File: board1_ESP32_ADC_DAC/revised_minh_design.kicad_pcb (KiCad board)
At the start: 2 copper layers, 137.7 x 59.9 mm, 15 parts, among them J1 Conn_01x03_Male, J2 Conn_01x07_Male, U1 ESP32-DevKit-C, U2 LM7805_TO220, U3 NE5532, U4 CB101

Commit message: -
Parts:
- removed C3: 0.1uF, Capacitor_THT:C_Disc_D6.0mm_W2.5mm_P5.00mm
- removed D1: TZX3V6A-TR, Diode_THT:D_DO-35_SOD27_P7.62mm_Horizontal
- removed D2: LED, LED_THT:LED_D3.0mm_Clear
- removed J2: Conn_01x07_Male, Connector_PinSocket_2.54mm:PinSocket_1x07_P2.54mm_Vertical
- removed R1, R2: 10k, Resistor_THT:R_Axial_DIN0309_L9.0mm_D3.2mm_P15.24mm_Horizontal
- removed R3: 1K, Resistor_THT:R_Axial_DIN0309_L9.0mm_D3.2mm_P15.24mm_Horizontal
- removed R4: 4.7k, Resistor_THT:R_Axial_DIN0309_L9.0mm_D3.2mm_P15.24mm_Horizontal
- removed U3: NE5532, Package_DIP:DIP-8_W7.62mm
- removed U4: CB101, Library:CB101
- moved J1 70.2 mm to (40.0, 10.0), turned to 0 degrees
- moved C2 65.8 mm to (25.0, 20.0), turned to 0 degrees
- moved C1 55.6 mm to (55.0, 15.0), turned to 0 degrees
- moved U1 51.6 mm to (84.5, 81.2), turned to 90 degrees
- moved U2 34.7 mm to (24.9, 82.6)
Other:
- board size 137.7 x 59.9 mm -> 100 x 100 mm
- board text removed: "+12V"

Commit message: ADC_DAC
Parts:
- added C10: 2.2uF, Capacitor_SMD:C_0805_2012Metric_Pad1.18x1.45mm_HandSolder, F.Cu at (101.8, 49.1)
- added C11: 0.1uF, Capacitor_SMD:C_0805_2012Metric_Pad1.18x1.45mm_HandSolder, F.Cu at (113.9, 66.9)
- added C12: 2.2uF, Capacitor_SMD:C_0805_2012Metric_Pad1.18x1.45mm_HandSolder, F.Cu at (108.3, 43.8)
- added C13: 1nF, Capacitor_SMD:C_0805_2012Metric_Pad1.18x1.45mm_HandSolder, F.Cu at (111.2, 49.6)
- added C14: 1uF, Capacitor_SMD:C_0805_2012Metric_Pad1.18x1.45mm_HandSolder, F.Cu at (130.6, 51.4)
- added C3: 10uF, Capacitor_SMD:C_0805_2012Metric_Pad1.18x1.45mm_HandSolder, B.Cu at (108.0, 62.3)
- added C4: 0.1uF, Capacitor_SMD:C_0805_2012Metric_Pad1.18x1.45mm_HandSolder, B.Cu at (104.2, 53.7)
- added C5: 0.1uF, Capacitor_SMD:C_0805_2012Metric_Pad1.18x1.45mm_HandSolder, B.Cu at (106.0, 62.3)
- added C6: 0.1uF, Capacitor_SMD:C_0805_2012Metric_Pad1.18x1.45mm_HandSolder, B.Cu at (107.2, 56.4)
- added C7: 0.1uF, Capacitor_SMD:C_0805_2012Metric_Pad1.18x1.45mm_HandSolder, B.Cu at (106.0, 66.1)
- added C8: 10uF, Capacitor_SMD:C_0805_2012Metric_Pad1.18x1.45mm_HandSolder, B.Cu at (109.2, 56.4)
- added C9: 10uF, Capacitor_SMD:C_0805_2012Metric_Pad1.18x1.45mm_HandSolder, B.Cu at (108.0, 66.1)
- added J2: Conn_01x08_Male, Connector_PinSocket_2.54mm:PinSocket_1x08_P2.54mm_Vertical, F.Cu at (115.9, 42.4)
- added J3: Conn_01x08_Male, Connector_PinSocket_2.54mm:PinSocket_1x08_P2.54mm_Vertical, F.Cu at (120.8, 76.0)
- added J4: Conn_01x08_Male, Connector_PinSocket_2.54mm:PinSocket_1x08_P2.54mm_Vertical, F.Cu at (141.1, 48.6)
- added R1: 0, Resistor_SMD:R_0805_2012Metric_Pad1.20x1.40mm_HandSolder, B.Cu at (97.7, 56.5)
- added R2: 50, Resistor_SMD:R_0805_2012Metric_Pad1.20x1.40mm_HandSolder, F.Cu at (111.2, 45.9)
- added R3: 0, Resistor_SMD:R_0805_2012Metric_Pad1.20x1.40mm_HandSolder, F.Cu at (120.2, 65.9)
- added R4: 0, Resistor_SMD:R_0805_2012Metric_Pad1.20x1.40mm_HandSolder, F.Cu at (129.5, 47.6)
- added U3: MCP1754S-3302xCB, Package_TO_SOT_SMD:SOT-23, B.Cu at (104.2, 56.5)
- added U4: MCP1825S-3.3V, Package_TO_SOT_SMD:SOT-223-3_TabPin2, B.Cu at (100.6, 64.0)
- added U5: MCP1501-33xSN, Package_SO:SOIC-8_3.9x4.9mm_P1.27mm, F.Cu at (106.5, 47.5)
- added U6: MCP3464R, Package_SO:TSSOP-20_4.4x6.5mm_P0.65mm, F.Cu at (133.1, 57.1)
- added U7: MCP3464R, Package_SO:TSSOP-20_4.4x6.5mm_P0.65mm, F.Cu at (128.6, 68.7)
- added U8: DAC8568IAPW, Package_SO:TSSOP-16-1EP_4.4x5mm_P0.65mm, F.Cu at (124.0, 50.4)
- added X1: ECS-2520MVLC-049-BN-TR, Oscillator:Oscillator_SMD_ECS_2520MV-xxx-xx-4Pin_2.5x2.0mm, F.Cu at (116.6, 66.6)
- C1, C2: footprint Capacitor_THT:C_Disc_D6.0mm_W2.5mm_P5.00mm -> Capacitor_SMD:C_0805_2012Metric_Pad1.18x1.45mm_HandSolder
- moved J1 94.4 mm to (108.6, 74.9), turned to 90 degrees
- moved C2 90.4 mm to (98.8, 72.2)
- moved U2 78.9 mm to (103.4, 74.8), turned to 180 degrees
- moved C1 74.4 mm to (102.6, 72.2), turned to 180 degrees
- moved U1 31.1 mm to (65.0, 57.0)
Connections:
- U1 pad 25: unconnected-(U1-Pad25) -> MDAT
- U1 pad 26: unconnected-(U1-Pad26) -> ~{ADC2_CS}
- U1 pad 27: unconnected-(U1-Pad27) -> ~{ADC1_CS}
- U1 pad 28: DAC_SIG -> unconnected-(U1-Pad28)
- U1 pad 30: unconnected-(U1-Pad30) -> ~{DAC_CS}
- U1 pad 31: unconnected-(U1-Pad31) -> SK
- U1 pad 32: unconnected-(U1-Pad32) -> SI
- U1 pad 34: unconnected-(U1-Pad34) -> SO
- U1 pad 8: unconnected-(U1-Pad8) -> LDAC
- U1 pad 9: unconnected-(U1-Pad9) -> ~{CLR}
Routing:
- net ~{DAC_CS}: track 0.00 -> 50.1 mm
- net SK: track 0.00 -> 46.9 mm
- net SI: track 0.00 -> 44.7 mm
- net SO: track 0.00 -> 39.5 mm
- net +5V: track 0.00 -> 26.0 mm, vias 0 -> 3
- net GNDA: track 0.00 -> 19.5 mm, vias 0 -> 5
- net Earth: track 0.00 -> 16.6 mm, vias 0 -> 10
- net VoutA: track 0.00 -> 13.6 mm, vias 0 -> 1
- net ADC2_8: track 0.00 -> 13.3 mm, vias 0 -> 1
- net VoutB: track 0.00 -> 12.7 mm
- net ADC2_7: track 0.00 -> 12.0 mm
- net ADC2_1: track 0.00 -> 11.0 mm
- net VoutC: track 0.00 -> 10.7 mm, vias 0 -> 1
- net VoutD: track 0.00 -> 10.2 mm
- net VoutF: track 0.00 -> 9.68 mm
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- added copper zone on B.Cu, net Earth
- added copper zone on In1.Cu, net Earth
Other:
- board size 100 x 100 mm -> 94 x 39 mm
- copper layers 2 -> 4

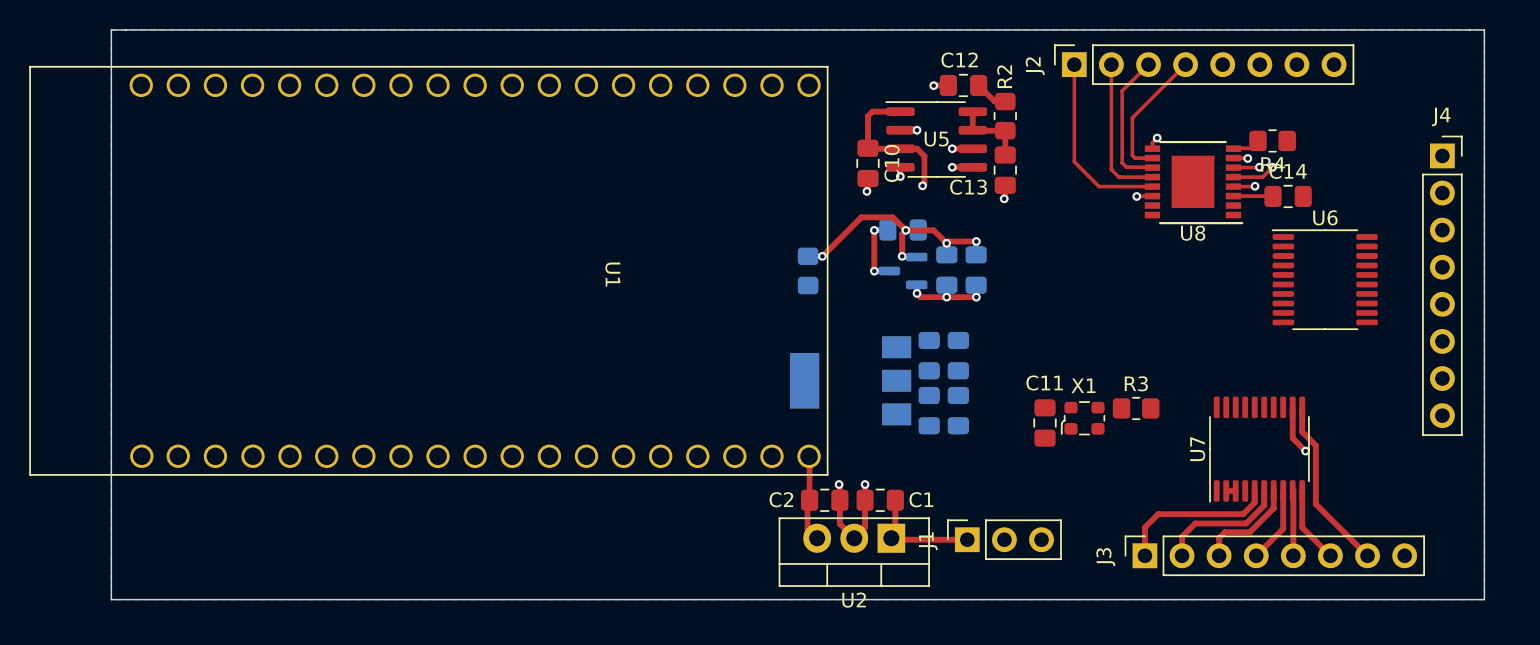
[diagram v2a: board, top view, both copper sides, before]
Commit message: components routing mostly finished for DAC/ADC board
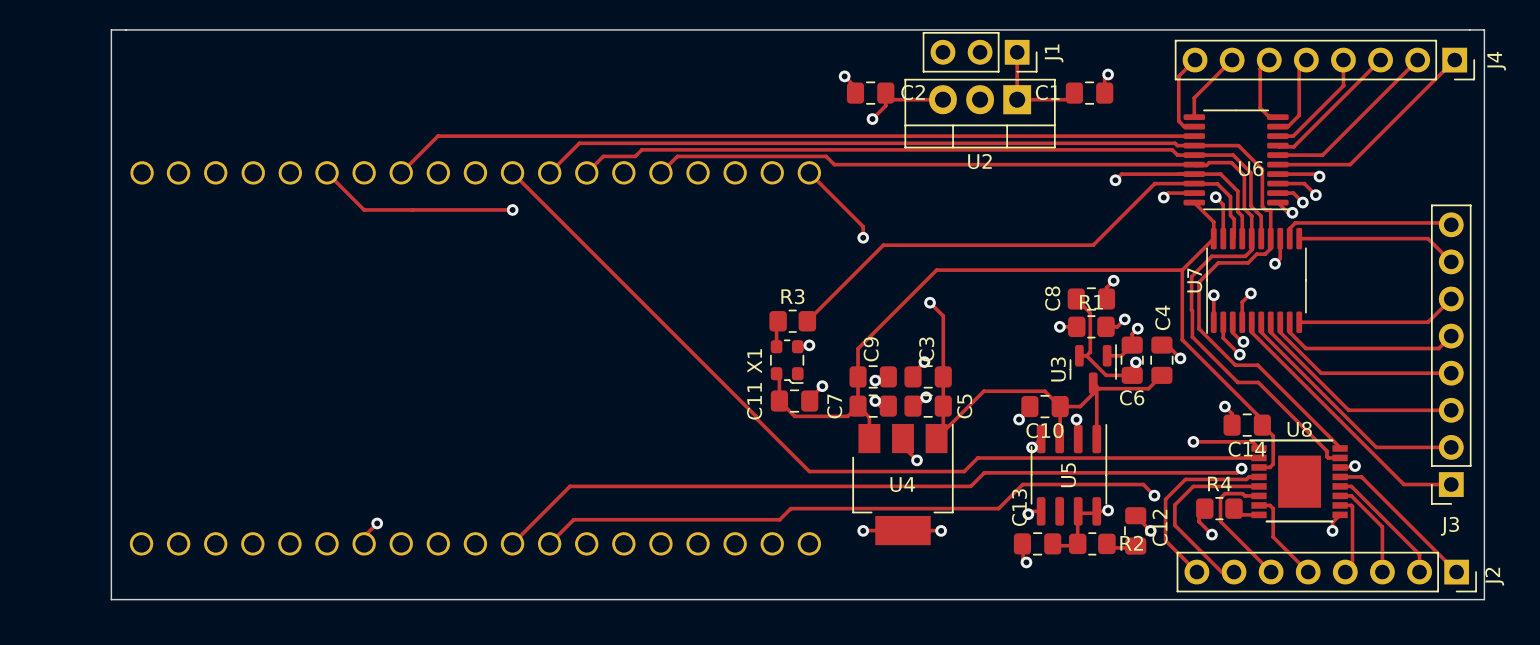
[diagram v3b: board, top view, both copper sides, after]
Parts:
- C3, C4, C5, C6, C7, C8, C9, R1, U3, U4: moved to F.Cu
- U1: moved to B.Cu
- moved J2 43.5 mm to (142.1, 77.1), turned to -90 degrees
- moved J1 33.5 mm to (112.0, 41.5), turned to -90 degrees
- moved C12 32.7 mm to (120.1, 74.3), turned to 90 degrees
- moved C1 31.3 mm to (117.0, 44.3), turned to 0 degrees
- moved U2 31.2 mm to (112.0, 44.8)
- moved R2 29.9 mm to (117.2, 75.2), turned to 0 degrees
- moved C2 28.1 mm to (102.0, 44.3), turned to 180 degrees
- moved C13 25.7 mm to (113.4, 75.2), turned to 180 degrees
- moved R4 25.4 mm to (125.9, 72.8), turned to 0 degrees
- moved U5 24.7 mm to (115.6, 70.5), turned to -90 degrees
- moved R3 24.3 mm to (96.6, 59.9)
- moved U8 21.8 mm to (131.3, 70.9), turned to 0 degrees
- moved J3 21.5 mm to (141.7, 71.1), turned to 180 degrees
- moved X1 20.7 mm to (96.3, 62.6), turned to 180 degrees
- moved C10 20.6 mm to (113.9, 65.8), turned to 180 degrees
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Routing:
- net MDAT: track 0.00 -> 70.9 mm, vias 0 -> 2
- net ~{ADC2_CS}: track 0.00 -> 68.7 mm, vias 0 -> 1
- net +3V3: track 2.71 -> 62.0 mm
- net ~{ADC1_CS}: track 0.00 -> 55.3 mm
- net ~{CLR}: track 7.06 -> 61.3 mm, vias 1 -> 2
- net LDAC: track 0.00 -> 52.9 mm, vias 0 -> 2
- net +3.3VDAC: track 5.17 -> 51.5 mm, vias 0 -> 4
- net CLK: track 0.00 -> 36.3 mm
- net +5V: track 26.0 -> 58.7 mm
- net SK: track 46.9 -> 78.4 mm
- net SO: track 39.5 -> 69.2 mm
- net +3.3VA: track 6.42 -> 29.7 mm
- net Earth: track 16.6 -> 34.7 mm, vias 10 -> 23
- net ADC1_1: track 0.00 -> 15.1 mm
- net ADC1_2: track 0.00 -> 12.3 mm
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- added copper zone on In1.Cu, net GNDA
- removed copper zone on B.Cu, net Earth

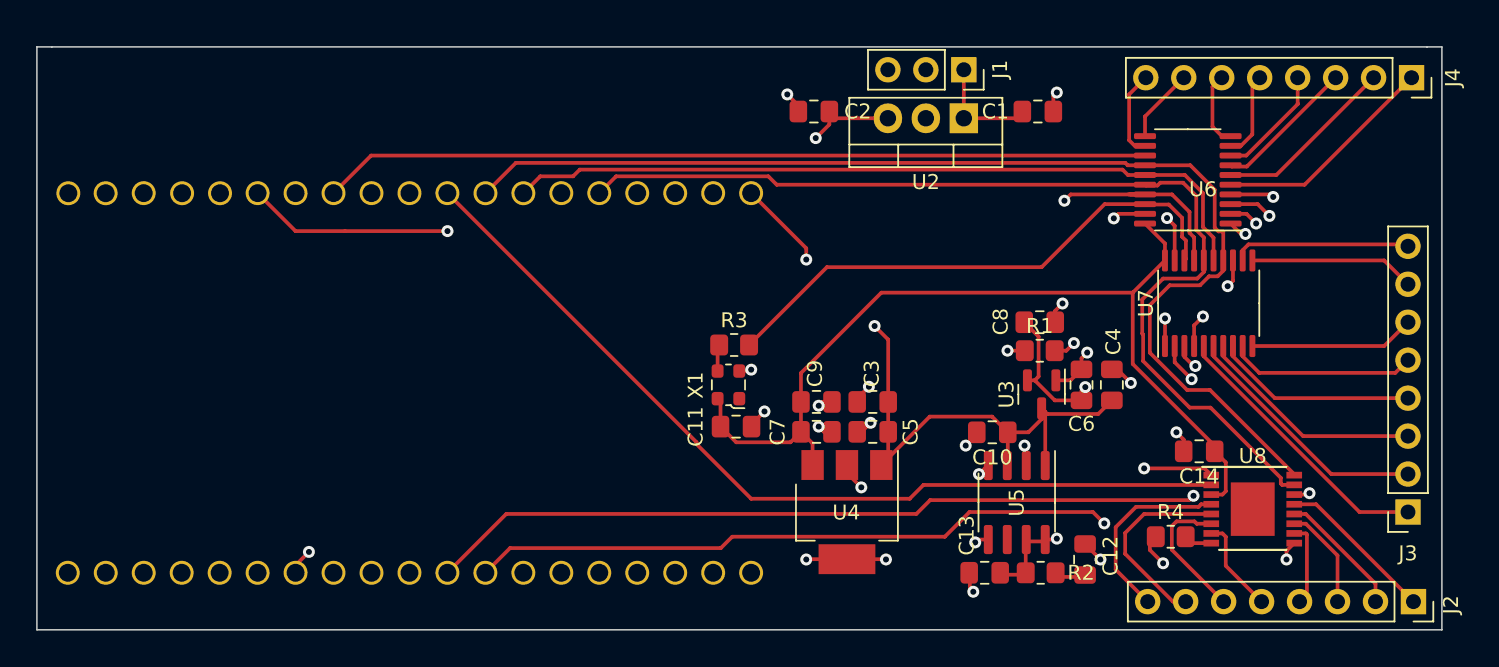
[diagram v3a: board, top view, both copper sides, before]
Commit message: components routing mostly finished for DAC/ADC board
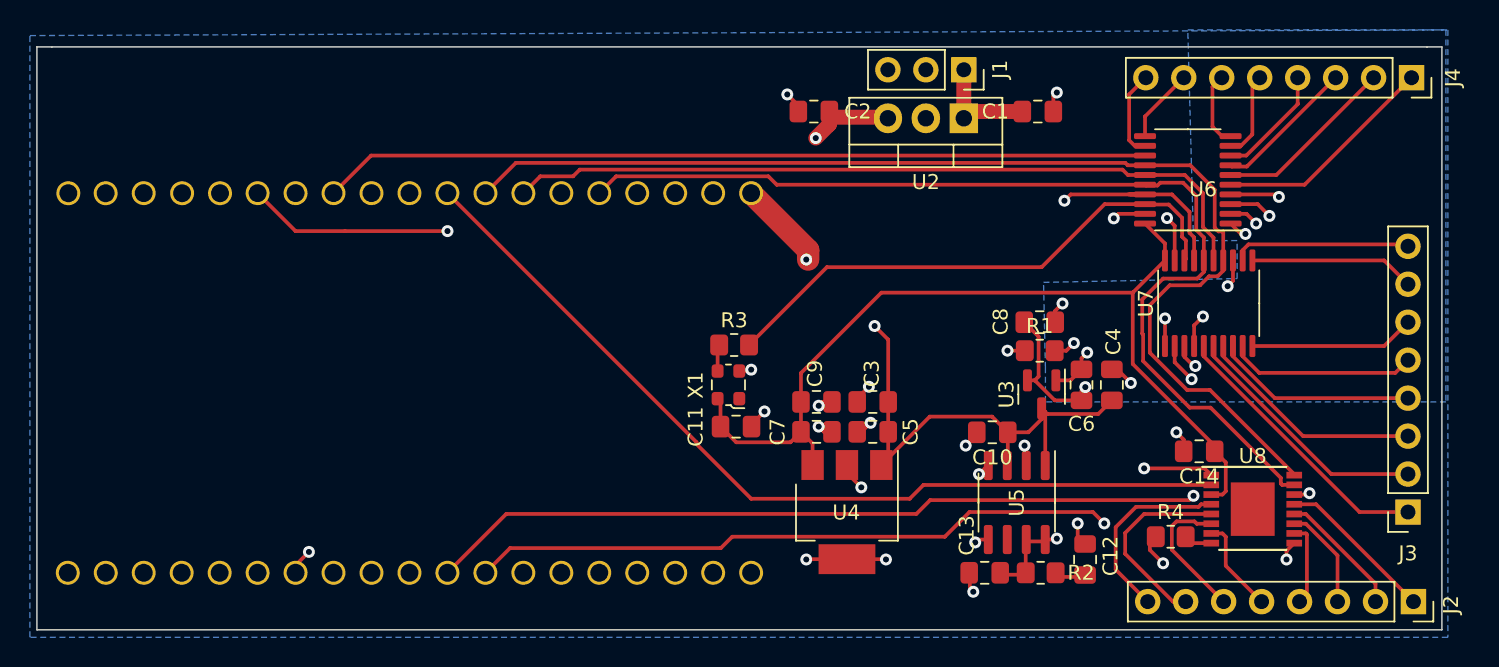
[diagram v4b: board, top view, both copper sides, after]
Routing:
- net +12V: track 7.35 -> 7.99 mm
- added copper zone on In2.Cu, net +12V
- added copper zone on In2.Cu, net +3.3VDAC
- added copper zone on In2.Cu, net +5V
- added copper zone on B.Cu, net Earth
- added copper zone on B.Cu, net GNDA

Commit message: minor adjustments
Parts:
- moved C8 0.15 mm to (117.0, 58.3)
- moved C3 0.13 mm to (105.9, 63.9)
- moved C9 0.13 mm to (102.2, 63.9)
- moved U4 0.13 mm to (104.2, 71.2)
- moved C5 0.13 mm to (105.9, 65.9)
- moved C7 0.13 mm to (102.2, 65.9)
- moved R1 0.05 mm to (117.0, 60.3)
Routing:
- net +12V: track 7.99 -> 2.76 mm, vias 0 -> 1
- net GNDA: track 17.2 -> 19.1 mm
- net Earth: track 34.8 -> 36.0 mm, vias 23 -> 24

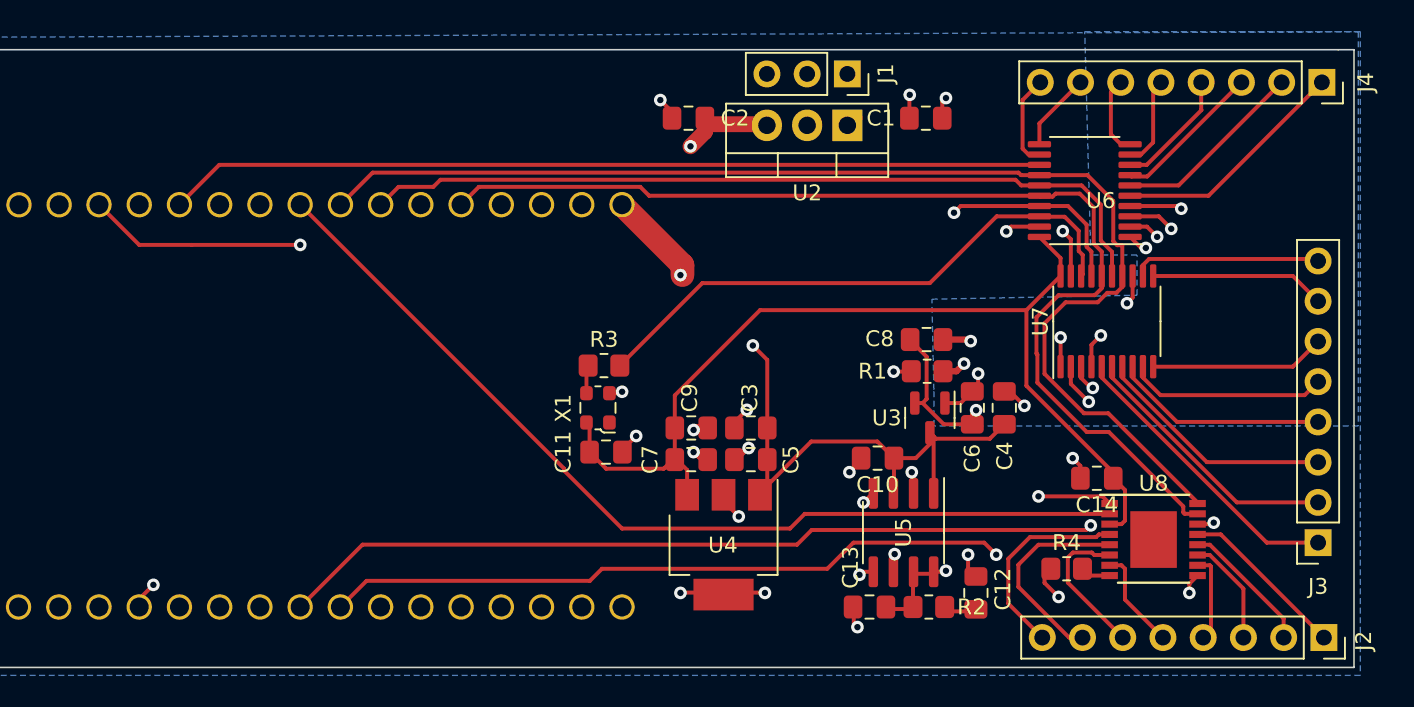
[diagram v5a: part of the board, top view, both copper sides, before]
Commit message: resolved DRC errors and most warnings
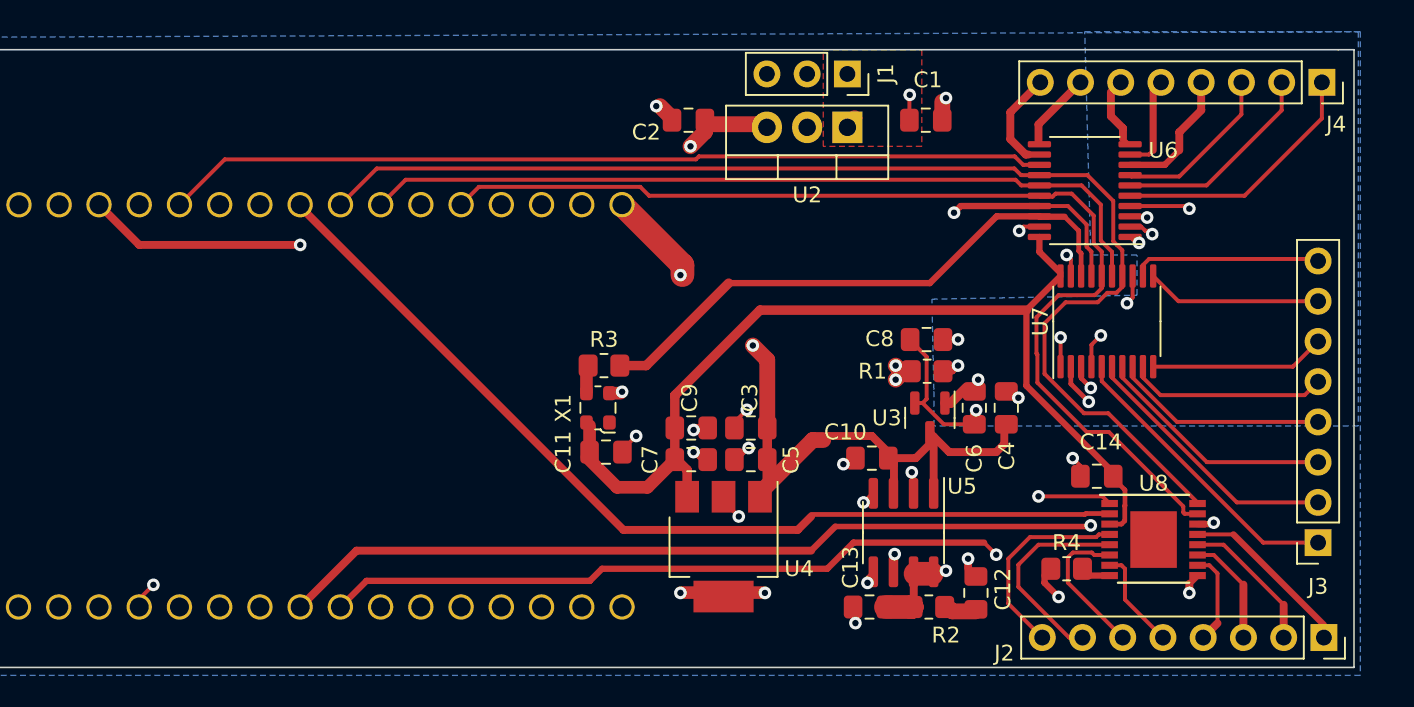
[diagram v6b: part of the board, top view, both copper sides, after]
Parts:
- moved C10 0.36 mm to (113.6, 65.8)
- moved C1 0.13 mm to (117.0, 44.5)
- moved C2 0.13 mm to (102.0, 44.5)
- moved U2 0.13 mm to (112.0, 44.9)
- moved C14 0.13 mm to (127.8, 66.9)
- moved C4 0.13 mm to (122.0, 62.6)
- moved C6 0.13 mm to (120.0, 62.6)
- moved U4 0.12 mm to (104.2, 71.4)
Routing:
- net GNDA: track 19.1 -> 13.4 mm
- net Earth: track 36.0 -> 34.1 mm, vias 24 -> 25
- net +5V: track 58.5 -> 60.3 mm
- net ADC1_1: track 15.1 -> 16.4 mm
- net ADC1_3: track 9.53 -> 10.7 mm
- net ADC1_2: track 12.3 -> 13.3 mm
- net +3.3VDAC: track 51.7 -> 50.8 mm
- net ADC1_8: track 5.86 -> 6.61 mm
- net ADC1_4: track 7.69 -> 8.36 mm
- net +3V3: track 62.0 -> 62.5 mm
- net VoutD: track 8.57 -> 9.08 mm
- added copper zone on F.Cu, net +12V
